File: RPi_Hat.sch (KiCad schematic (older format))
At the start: 4 parts

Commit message: Improve schems
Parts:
- gave numbers to parts that had none: 4
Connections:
- net +12V: now reaches C1.1, J1.1 (Pin_1), U1.3 (VI)
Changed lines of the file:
@@
 $EndSheet
 $Comp
-L Regulator_Linear:LM1085-5.0 U?
+L Regulator_Linear:LM1085-5.0 U1
 U 1 1 5C49FAC8
 P 7350 1900
-F 0 "U?" H 7350 2142 50  0000 C CNN
+F 0 "U1" H 7350 2142 50  0000 C CNN
 F 1 "LM1085-5.0" H 7350 2051 50  0000 C CNN
 F 2 "" H 7350 2150 50  0001 C CIN
@@
 $EndComp
 $Comp
-L Connector:Conn_01x02_Male J?
+L Connector:Conn_01x02_Male J1
 U 1 1 5C49FBAD
 P 6100 1900
-F 0 "J?" H 6206 2078 50  0000 C CNN
+F 0 "J1" H 6206 2078 50  0000 C CNN
 F 1 "Conn_01x02_Male" H 6206 1987 50  0000 C CNN
 F 2 "" H 6100 1900 50  0001 C CNN
@@
 	6300 1900 6750 1900
 $Comp
-L Device:C C?
+L Device:C C1
 U 1 1 5C49FDF3
 P 6750 2250
-F 0 "C?" H 6865 2296 50  0000 L CNN
+F 0 "C1" H 6865 2296 50  0000 L CNN
 F 1 "10uF" H 6865 2205 50  0000 L CNN
 F 2 "" H 6788 2100 50  0001 C CNN
@@
 $EndComp
 $Comp
-L Device:C C?
+L Device:C C2
 U 1 1 5C4A03AD
 P 8000 2250
-F 0 "C?" H 8115 2296 50  0000 L CNN
+F 0 "C2" H 8115 2296 50  0000 L CNN
 F 1 "100uF" H 8115 2205 50  0000 L CNN
 F 2 "" H 8038 2100 50  0001 C CNN
@@
 Wire Wire Line
 	8000 2500 8000 2400
+Wire Wire Line
+	6750 1900 6750 1750
+$Comp
+L power:+12V #PWR?
+U 1 1 5C6E2F5B
+P 6750 1750
+F 0 "#PWR?" H 6750 1600 50  0001 C CNN
+F 1 "+12V" H 6765 1923 50  0000 C CNN
+F 2 "" H 6750 1750 50  0001 C CNN
+F 3 "" H 6750 1750 50  0001 C CNN
+	1    6750 1750
+	1    0    0    -1
+$EndComp
 $EndSCHEMATC

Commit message: Start to fill components footprints and dkRef
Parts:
- C1: footprint (none) -> Inductors_SMD:L_0805_HandSoldering; dkReference (none) -> 1276-2405-1-ND
- U1: footprint (none) -> TO_SOT_Packages_SMD:TO-263-4; dkReference (none) -> 296-35391-1-ND
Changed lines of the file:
@@
 F 0 "U1" H 7350 2142 50  0000 C CNN
 F 1 "LM1085-5.0" H 7350 2051 50  0000 C CNN
-F 2 "" H 7350 2150 50  0001 C CIN
+F 2 "TO_SOT_Packages_SMD:TO-263-4" H 7350 2150 50  0001 C CIN
 F 3 "http://www.ti.com/lit/ds/symlink/lm1085.pdf" H 7350 1900 50  0001 C CNN
+F 4 "296-35391-1-ND" H 7350 1900 50  0001 C CNN "dkReference"
 	1    7350 1900
 	1    0    0    -1
@@
 F 0 "C1" H 6865 2296 50  0000 L CNN
 F 1 "10uF" H 6865 2205 50  0000 L CNN
-F 2 "" H 6788 2100 50  0001 C CNN
+F 2 "Inductors_SMD:L_0805_HandSoldering" H 6788 2100 50  0001 C CNN
 F 3 "~" H 6750 2250 50  0001 C CNN
+F 4 "1276-2405-1-ND" H 6750 2250 50  0001 C CNN "dkReference"
 	1    6750 2250
 	1    0    0    -1

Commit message: Change components ref and package
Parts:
- C2: footprint (none) -> Capacitors_SMD:C_1206_HandSoldering; dkReference (none) -> 490-13982-1-ND
- J1: dkReference (none) -> ED2819-ND
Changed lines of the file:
@@
 F 2 "" H 6100 1900 50  0001 C CNN
 F 3 "~" H 6100 1900 50  0001 C CNN
+F 4 "ED2819-ND" H 0   0   50  0001 C CNN "dkReference"
 	1    6100 1900
 	1    0    0    -1
@@
 F 0 "C2" H 8115 2296 50  0000 L CNN
 F 1 "100uF" H 8115 2205 50  0000 L CNN
-F 2 "" H 8038 2100 50  0001 C CNN
+F 2 "Capacitors_SMD:C_1206_HandSoldering" H 8038 2100 50  0001 C CNN
 F 3 "~" H 8000 2250 50  0001 C CNN
+F 4 "490-13982-1-ND" H 8000 2250 50  0001 C CNN "dkReference"
 	1    8000 2250
 	1    0    0    -1

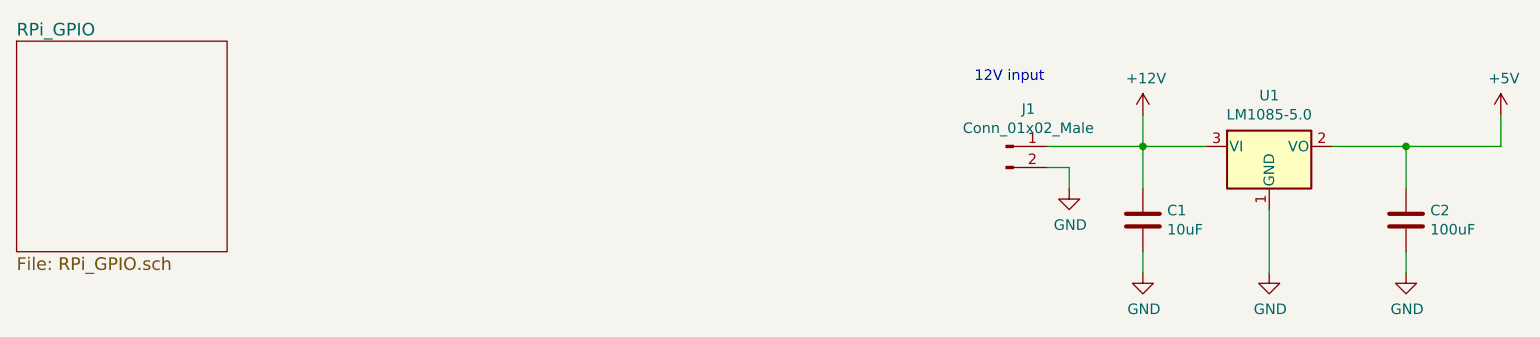
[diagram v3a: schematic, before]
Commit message: Correct DRC and add nmea interface
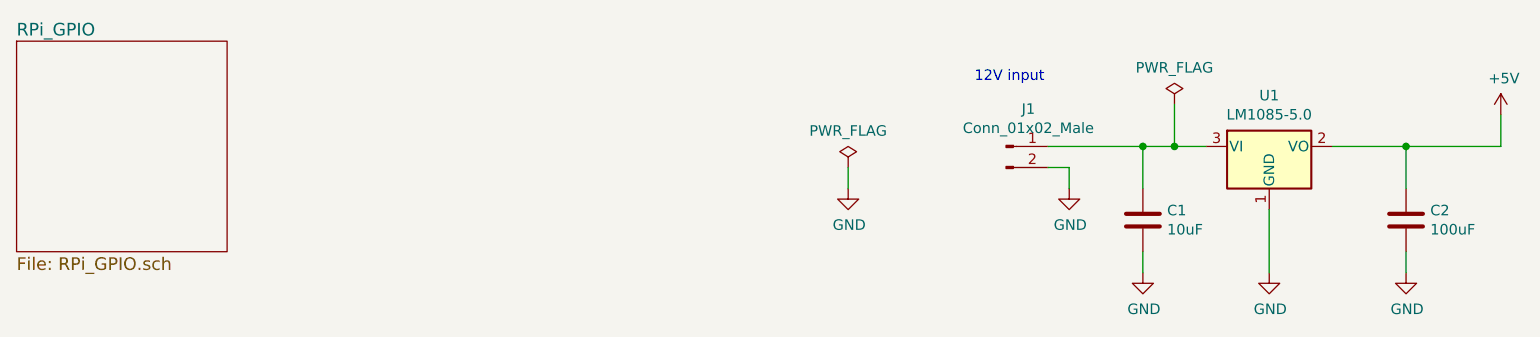
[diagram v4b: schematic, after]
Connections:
- net +12V: no longer names the net of C1.1, J1.1 (Pin_1), U1.3 (VI)
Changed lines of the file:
@@
 Connection ~ 6750 1900
 Wire Wire Line
-	6750 1900 7050 1900
+	6750 1900 6900 1900
 Wire Wire Line
 	6300 2000 6400 2000
@@
 	1    0    0    -1
 $EndComp
-Wire Wire Line
-	7350 2200 7350 2500
 $Comp
 L power:GND #PWR?
@@
 Wire Wire Line
 	8000 2500 8000 2400
-Wire Wire Line
-	6750 1900 6750 1750
 $Comp
-L power:+12V #PWR?
-U 1 1 5C6E2F5B
-P 6750 1750
-F 0 "#PWR?" H 6750 1600 50  0001 C CNN
-F 1 "+12V" H 6765 1923 50  0000 C CNN
-F 2 "" H 6750 1750 50  0001 C CNN
-F 3 "" H 6750 1750 50  0001 C CNN
-	1    6750 1750
+L power:PWR_FLAG #FLG?
+U 1 1 5C7100A3
+P 6900 1700
+F 0 "#FLG?" H 6900 1775 50  0001 C CNN
+F 1 "PWR_FLAG" H 6900 1874 50  0000 C CNN
+F 2 "" H 6900 1700 50  0001 C CNN
+F 3 "~" H 6900 1700 50  0001 C CNN
+	1    6900 1700
 	1    0    0    -1
 $EndComp
+Wire Wire Line
+	6900 1700 6900 1900
+Connection ~ 6900 1900
+Wire Wire Line
+	6900 1900 7050 1900
+Wire Wire Line
+	7350 2200 7350 2500
+$Comp
+L power:PWR_FLAG #FLG?
+U 1 1 5C710DD4
+P 5350 2000
+F 0 "#FLG?" H 5350 2075 50  0001 C CNN
+F 1 "PWR_FLAG" H 5350 2174 50  0000 C CNN
+F 2 "" H 5350 2000 50  0001 C CNN
+F 3 "~" H 5350 2000 50  0001 C CNN
+	1    5350 2000
+	1    0    0    -1
+$EndComp
+Wire Wire Line
+	5350 2000 5350 2100
+$Comp
+L power:GND #PWR?
+U 1 1 5C710F43
+P 5350 2100
+F 0 "#PWR?" H 5350 1850 50  0001 C CNN
+F 1 "GND" H 5355 1927 50  0000 C CNN
+F 2 "" H 5350 2100 50  0001 C CNN
+F 3 "" H 5350 2100 50  0001 C CNN
+	1    5350 2100
+	1    0    0    -1
+$EndComp

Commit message: Finish schem and start routing
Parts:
- J1: footprint (none) -> Connectors_JST:JST_SH_SM02B-SRSS-TB_02x1.00mm_Angled; dkReference ED2819-ND -> 455-1802-1-ND
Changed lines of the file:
@@
 F 0 "J1" H 6206 2078 50  0000 C CNN
 F 1 "Conn_01x02_Male" H 6206 1987 50  0000 C CNN
-F 2 "" H 6100 1900 50  0001 C CNN
+F 2 "Connectors_JST:JST_SH_SM02B-SRSS-TB_02x1.00mm_Angled" H 6100 1900 50  0001 C CNN
 F 3 "~" H 6100 1900 50  0001 C CNN
-F 4 "ED2819-ND" H 0   0   50  0001 C CNN "dkReference"
+F 4 "455-1802-1-ND" H 0   0   50  0001 C CNN "dkReference"
 	1    6100 1900
 	1    0    0    -1

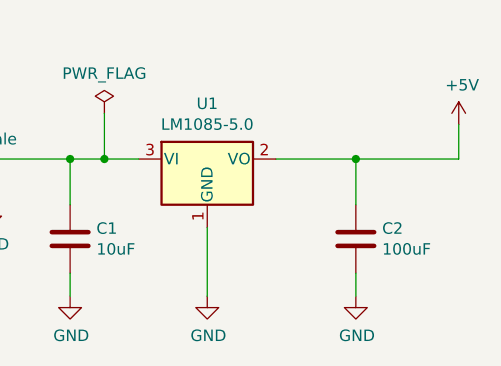
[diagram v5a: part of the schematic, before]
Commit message: Connect reset and boot0 to raspi and change few things
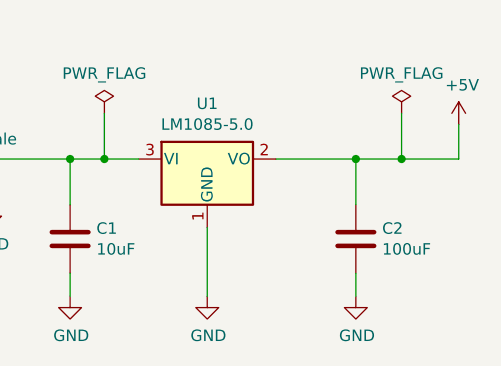
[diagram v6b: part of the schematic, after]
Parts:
- U1: footprint TO_SOT_Packages_SMD:TO-263-4 -> TO_SOT_Packages_SMD:TO-263-3_TabPin2
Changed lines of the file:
@@
 F 0 "U1" H 7350 2142 50  0000 C CNN
 F 1 "LM1085-5.0" H 7350 2051 50  0000 C CNN
-F 2 "TO_SOT_Packages_SMD:TO-263-4" H 7350 2150 50  0001 C CIN
+F 2 "TO_SOT_Packages_SMD:TO-263-3_TabPin2" H 7350 2150 50  0001 C CIN
 F 3 "http://www.ti.com/lit/ds/symlink/lm1085.pdf" H 7350 1900 50  0001 C CNN
 F 4 "296-35391-1-ND" H 7350 1900 50  0001 C CNN "dkReference"
@@
 Connection ~ 8000 1900
 Wire Wire Line
-	8000 1900 8450 1900
+	8000 1900 8200 1900
 Wire Wire Line
 	8000 2500 8000 2400
@@
 	1    0    0    -1
 $EndComp
+$Comp
+L power:PWR_FLAG #FLG?
+U 1 1 5C610BAB
+P 8200 1700
+F 0 "#FLG?" H 8200 1775 50  0001 C CNN
+F 1 "PWR_FLAG" H 8200 1874 50  0000 C CNN
+F 2 "" H 8200 1700 50  0001 C CNN
+F 3 "~" H 8200 1700 50  0001 C CNN
+	1    8200 1700
+	1    0    0    -1
+$EndComp
+Wire Wire Line
+	8200 1700 8200 1900
+Connection ~ 8200 1900
+Wire Wire Line
+	8200 1900 8450 1900
 $EndSCHEMATC

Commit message: Add terminaison resistors
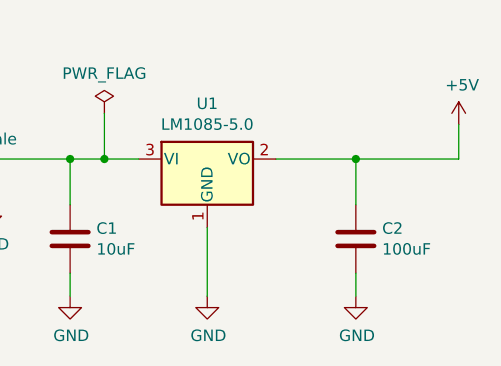
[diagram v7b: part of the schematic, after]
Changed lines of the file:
@@
 Connection ~ 8000 1900
-Wire Wire Line
-	8000 1900 8200 1900
 Wire Wire Line
 	8000 2500 8000 2400
@@
 	1    0    0    -1
 $EndComp
-$Comp
-L power:PWR_FLAG #FLG?
-U 1 1 5C610BAB
-P 8200 1700
-F 0 "#FLG?" H 8200 1775 50  0001 C CNN
-F 1 "PWR_FLAG" H 8200 1874 50  0000 C CNN
-F 2 "" H 8200 1700 50  0001 C CNN
-F 3 "~" H 8200 1700 50  0001 C CNN
-	1    8200 1700
-	1    0    0    -1
-$EndComp
 Wire Wire Line
-	8200 1700 8200 1900
-Connection ~ 8200 1900
-Wire Wire Line
-	8200 1900 8450 1900
+	8000 1900 8450 1900
 $EndSCHEMATC
